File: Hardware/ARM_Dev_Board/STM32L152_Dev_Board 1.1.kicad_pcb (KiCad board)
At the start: 2 copper layers, 65.3 x 24.5 mm, 21 parts, among them J1 SWD_Header, J2 Conn_01x20_Female, J3 Conn_01x22_Female, J4 Eurorack_10_pin_power, SW1 SW_Push, U1 STM32L451CCUx, U4 LM1117-3.3, Y1 Crystal

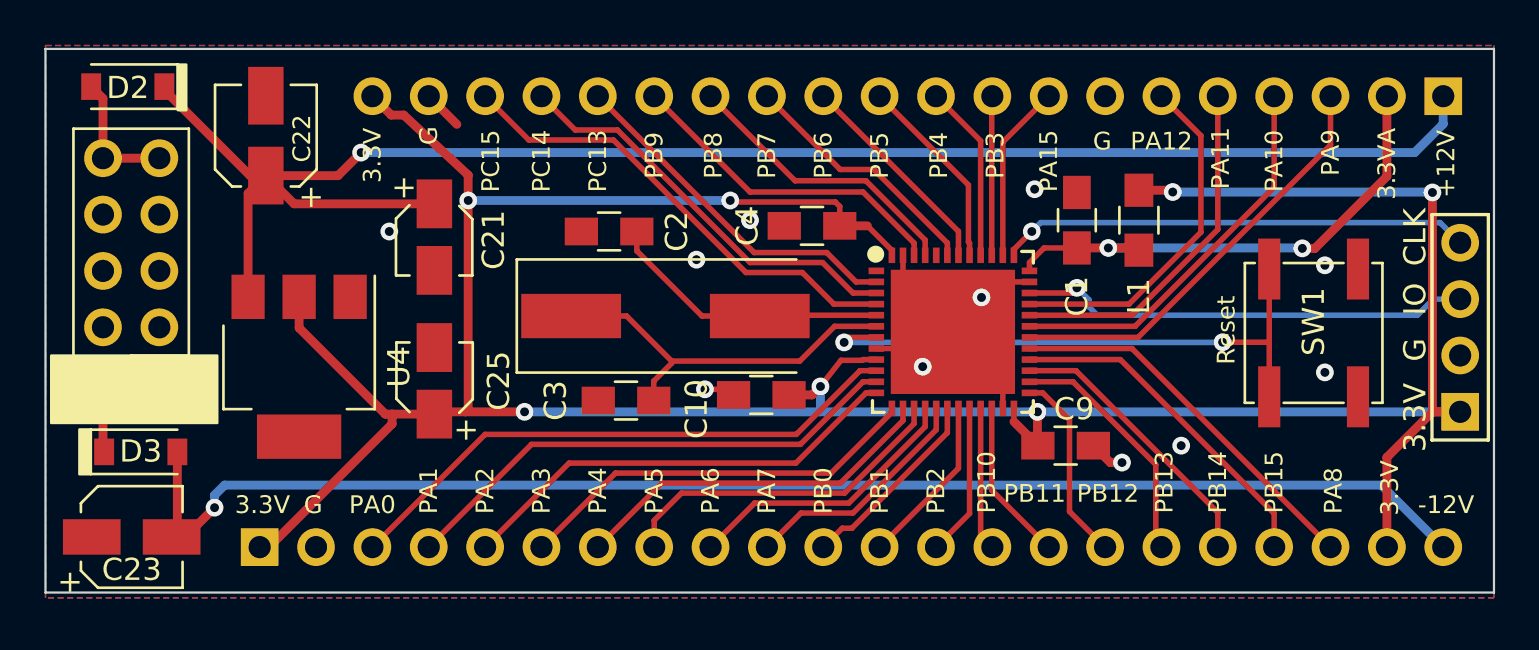
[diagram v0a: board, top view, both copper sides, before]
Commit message: Added early draft of support for ICE40UP5k FPGA
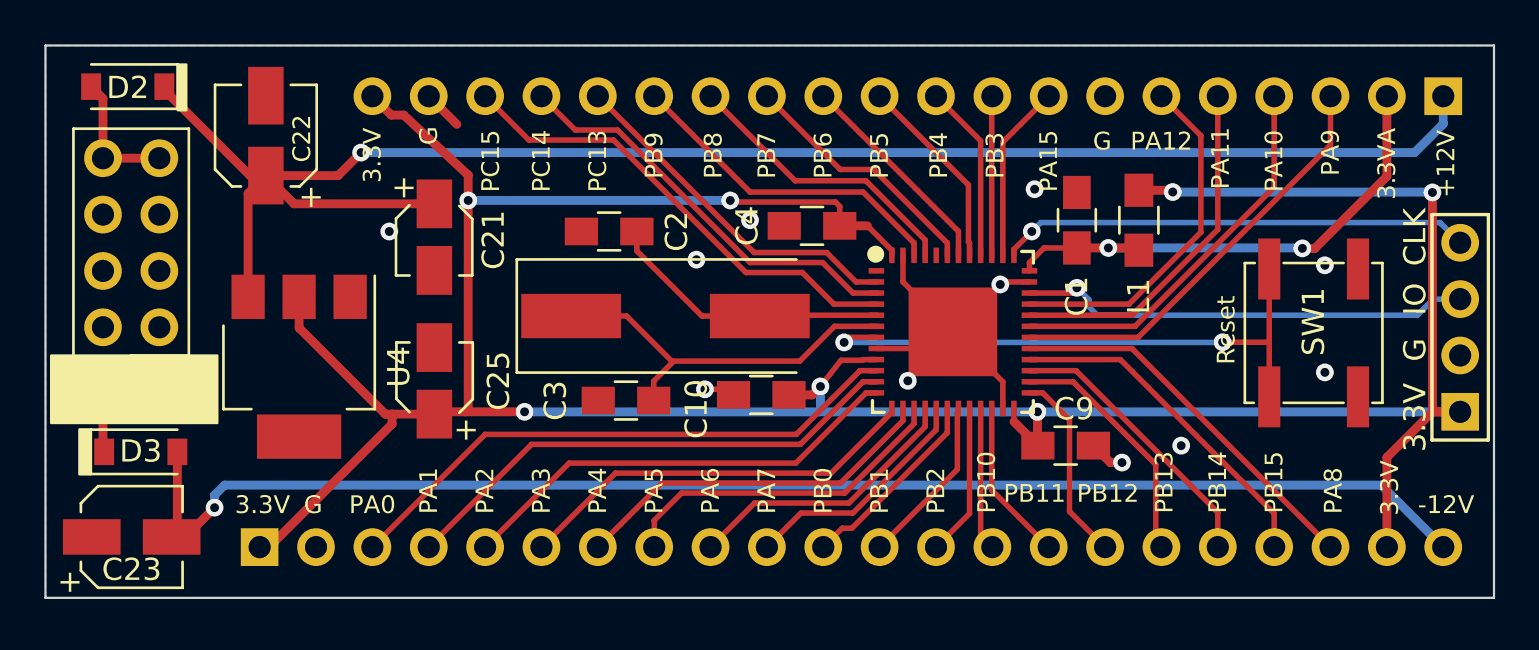
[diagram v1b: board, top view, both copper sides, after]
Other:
- board size 65.3 x 24.5 mm -> 65.3 x 24.9 mm
- board text added: "STM32L152 and STM32L451 Dev Board Mountjoy Modular v1.1"
- board text removed: "STM32L152 and STM32L451 Dev Board Mountjoy Modular v2.0"
